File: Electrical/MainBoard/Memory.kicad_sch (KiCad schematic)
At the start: 4 parts, among them J16 MEM2061-01-188-00-A, U11 M95M01-DFMN6TP

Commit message: Begin layout of pcb
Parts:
- renumbered J16 to J17, U11 to U15
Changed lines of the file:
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@@
   (symbol (lib_id "RobotLibary:MEM2061-01-188-00-A") (at 118.745 44.45 0) (unit 1)
     (in_bom yes) (on_board yes) (dnp no)
-    (property "Reference" "J16" (at 149.86 38.1 0)
+    (property "Reference" "J17" (at 149.86 38.1 0)
       (effects (font (size 1.524 1.524)))
     )
@@
       (project "MainBoard"
         (path "/bd24c4db-4e36-4117-bd4f-5228ef241da9/f4129289-3c0d-4adc-b4a9-f79af269c84f"
-          (reference "J16") (unit 1)
+          (reference "J17") (unit 1)
         )
       )
@@
         )
         (path "/bd24c4db-4e36-4117-bd4f-5228ef241da9/f4129289-3c0d-4adc-b4a9-f79af269c84f"
-          (reference "#PWR0124") (unit 1)
+          (reference "#PWR0155") (unit 1)
         )
       )
@@
   (symbol (lib_id "power:GND") (at 186.69 46.99 0) (unit 1)
     (in_bom yes) (on_board yes) (dnp no) (fields_autoplaced)
-    (property "Reference" "#PWR0120" (at 186.69 53.34 0)
+    (property "Reference" "#PWR0159" (at 186.69 53.34 0)
       (effects (font (size 1.27 1.27)) hide)
     )
@@
       (project "MainBoard"
         (path "/bd24c4db-4e36-4117-bd4f-5228ef241da9/f4129289-3c0d-4adc-b4a9-f79af269c84f"
-          (reference "#PWR0120") (unit 1)
+          (reference "#PWR0159") (unit 1)
         )
       )
@@
   (symbol (lib_id "power:GND") (at 113.03 41.275 0) (unit 1)
     (in_bom yes) (on_board yes) (dnp no)
-    (property "Reference" "#PWR0123" (at 113.03 47.625 0)
+    (property "Reference" "#PWR0151" (at 113.03 47.625 0)
       (effects (font (size 1.27 1.27)) hide)
     )
@@
       (project "MainBoard"
         (path "/bd24c4db-4e36-4117-bd4f-5228ef241da9/f4129289-3c0d-4adc-b4a9-f79af269c84f"
-          (reference "#PWR0123") (unit 1)
+          (reference "#PWR0151") (unit 1)
         )
       )
@@
         )
         (path "/bd24c4db-4e36-4117-bd4f-5228ef241da9/f4129289-3c0d-4adc-b4a9-f79af269c84f"
-          (reference "C22") (unit 1)
+          (reference "C36") (unit 1)
         )
       )
@@
   (symbol (lib_id "power:GND") (at 179.705 106.68 0) (unit 1)
     (in_bom yes) (on_board yes) (dnp no)
-    (property "Reference" "#PWR0130" (at 179.705 113.03 0)
+    (property "Reference" "#PWR0158" (at 179.705 113.03 0)
       (effects (font (size 1.27 1.27)) hide)
     )
@@
       (project "MainBoard"
         (path "/bd24c4db-4e36-4117-bd4f-5228ef241da9/f4129289-3c0d-4adc-b4a9-f79af269c84f"
-          (reference "#PWR0130") (unit 1)
+          (reference "#PWR0158") (unit 1)
         )
       )
@@
         )
         (path "/bd24c4db-4e36-4117-bd4f-5228ef241da9/f4129289-3c0d-4adc-b4a9-f79af269c84f"
-          (reference "#PWR0129") (unit 1)
+          (reference "#PWR0154") (unit 1)
         )
       )
@@
   (symbol (lib_id "power:+3.3V") (at 116.205 31.75 0) (unit 1)
     (in_bom yes) (on_board yes) (dnp no) (fields_autoplaced)
-    (property "Reference" "#PWR0122" (at 116.205 35.56 0)
+    (property "Reference" "#PWR0152" (at 116.205 35.56 0)
       (effects (font (size 1.27 1.27)) hide)
     )
@@
       (project "MainBoard"
         (path "/bd24c4db-4e36-4117-bd4f-5228ef241da9/f4129289-3c0d-4adc-b4a9-f79af269c84f"
-          (reference "#PWR0122") (unit 1)
+          (reference "#PWR0152") (unit 1)
         )
       )
@@
         )
         (path "/bd24c4db-4e36-4117-bd4f-5228ef241da9/f4129289-3c0d-4adc-b4a9-f79af269c84f"
-          (reference "#PWR0125") (unit 1)
+          (reference "#PWR0156") (unit 1)
         )
       )
@@
   (symbol (lib_id "power:GND") (at 117.475 58.42 0) (unit 1)
     (in_bom yes) (on_board yes) (dnp no) (fields_autoplaced)
-    (property "Reference" "#PWR0121" (at 117.475 64.77 0)
+    (property "Reference" "#PWR0153" (at 117.475 64.77 0)
       (effects (font (size 1.27 1.27)) hide)
     )
@@
       (project "MainBoard"
         (path "/bd24c4db-4e36-4117-bd4f-5228ef241da9/f4129289-3c0d-4adc-b4a9-f79af269c84f"
-          (reference "#PWR0121") (unit 1)
+          (reference "#PWR0153") (unit 1)
         )
       )
@@
         )
         (path "/bd24c4db-4e36-4117-bd4f-5228ef241da9/f4129289-3c0d-4adc-b4a9-f79af269c84f"
-          (reference "#PWR0128") (unit 1)
+          (reference "#PWR0157") (unit 1)
         )
       )
@@
   (symbol (lib_id "RobotLibary:M95M01-DFMN6TP") (at 128.905 109.855 0) (unit 1)
     (in_bom yes) (on_board yes) (dnp no) (fields_autoplaced)
-    (property "Reference" "U11" (at 149.225 100.33 0)
+    (property "Reference" "U15" (at 149.225 100.33 0)
       (effects (font (size 1.524 1.524)))
     )
@@
       (project "MainBoard"
         (path "/bd24c4db-4e36-4117-bd4f-5228ef241da9/f4129289-3c0d-4adc-b4a9-f79af269c84f"
-          (reference "U11") (unit 1)
+          (reference "U15") (unit 1)
         )
       )
@@
         )
         (path "/bd24c4db-4e36-4117-bd4f-5228ef241da9/f4129289-3c0d-4adc-b4a9-f79af269c84f"
-          (reference "C21") (unit 1)
-        )
-      )
+          (reference "C35") (unit 1)
+        )
+      )

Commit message: Made V0.2 revisions to Main Board
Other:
- company: (none) -> satomm@stanford.edu
- title: (none) -> MCU Controller
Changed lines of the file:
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@@
 (kicad_sch (version 20230121) (generator eeschema)
   (paper "A4")
+  (title_block
+    (title "MCU Controller")
+    (rev "0.2")
+    (company "satomm@stanford.edu")
+    (comment 1 "Department of Civil and Environmental Engineering")
+    (comment 2 "Engineering Informatics Group")
+    (comment 3 "Stanford University")
+    (comment 4 "Matthew Sato")
+  )
   (junction (at 186.69 46.99) (diameter 0) (color 0 0 0 0)
   )

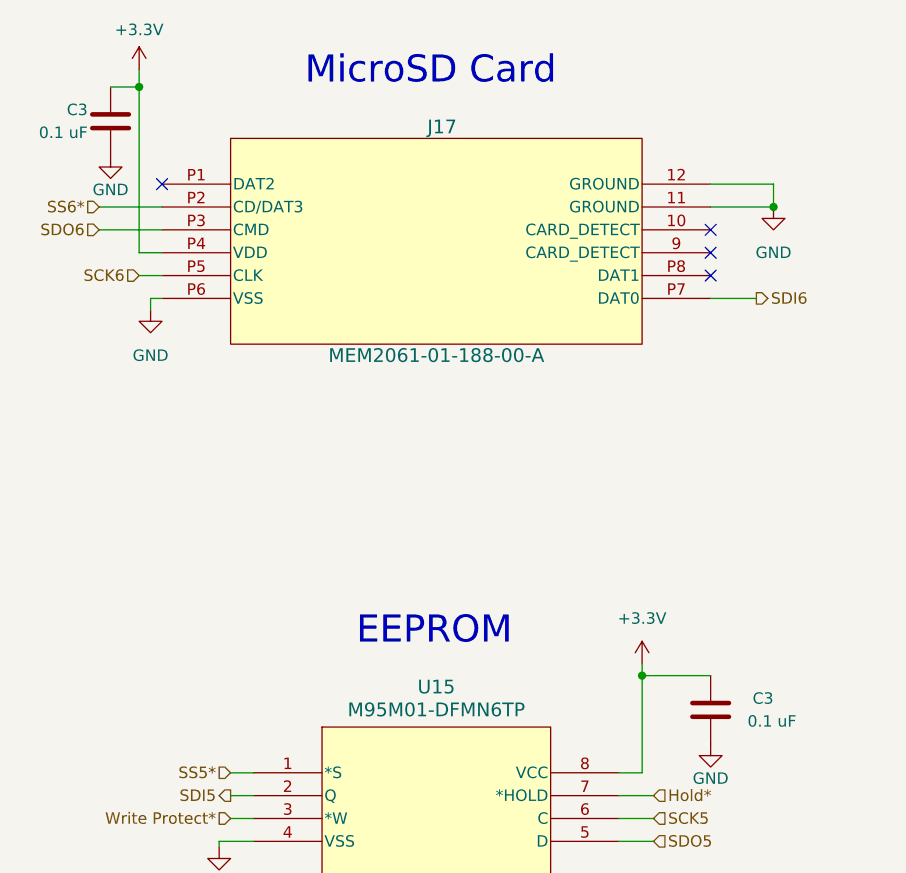
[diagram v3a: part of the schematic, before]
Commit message: Fix SPI3 and make visual improvements
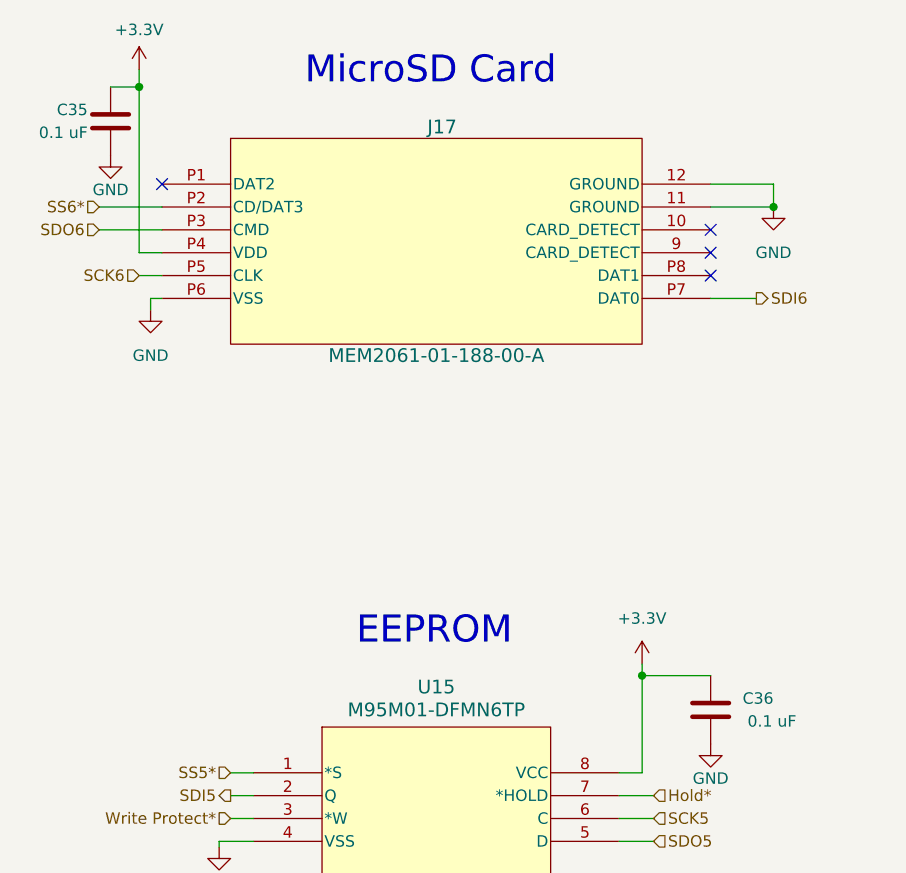
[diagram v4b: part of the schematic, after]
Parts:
- renumbered C3 to C35, C3 to C36

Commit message: Add updated pdf schematic
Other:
- moved on the sheet: C35, C36, J17, U15

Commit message: Update some parts
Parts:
- C35, J17: now left out of the parts list
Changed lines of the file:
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@@
 		(unit 1)
 		(exclude_from_sim no)
-		(in_bom yes)
+		(in_bom no)
 		(on_board yes)
 		(dnp no)
@@
 		(unit 1)
 		(exclude_from_sim no)
-		(in_bom yes)
-		(on_board yes)
-		(dnp no)
+		(in_bom no)
+		(on_board yes)
+		(dnp no)
